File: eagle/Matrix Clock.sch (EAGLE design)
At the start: 48 parts, among them IC1 MEGA32-A, IC2 LM1117IMPX-3.3, IC3 DS1307Z, IC4 MAX7219CWG, IC5 MAX7219CWG, IC6 MAX7219CWG, IC7 MAX7219CWG, Q1 32768, Q2 16MHz, X1 MINI-USB-SCHIELD-32005-301

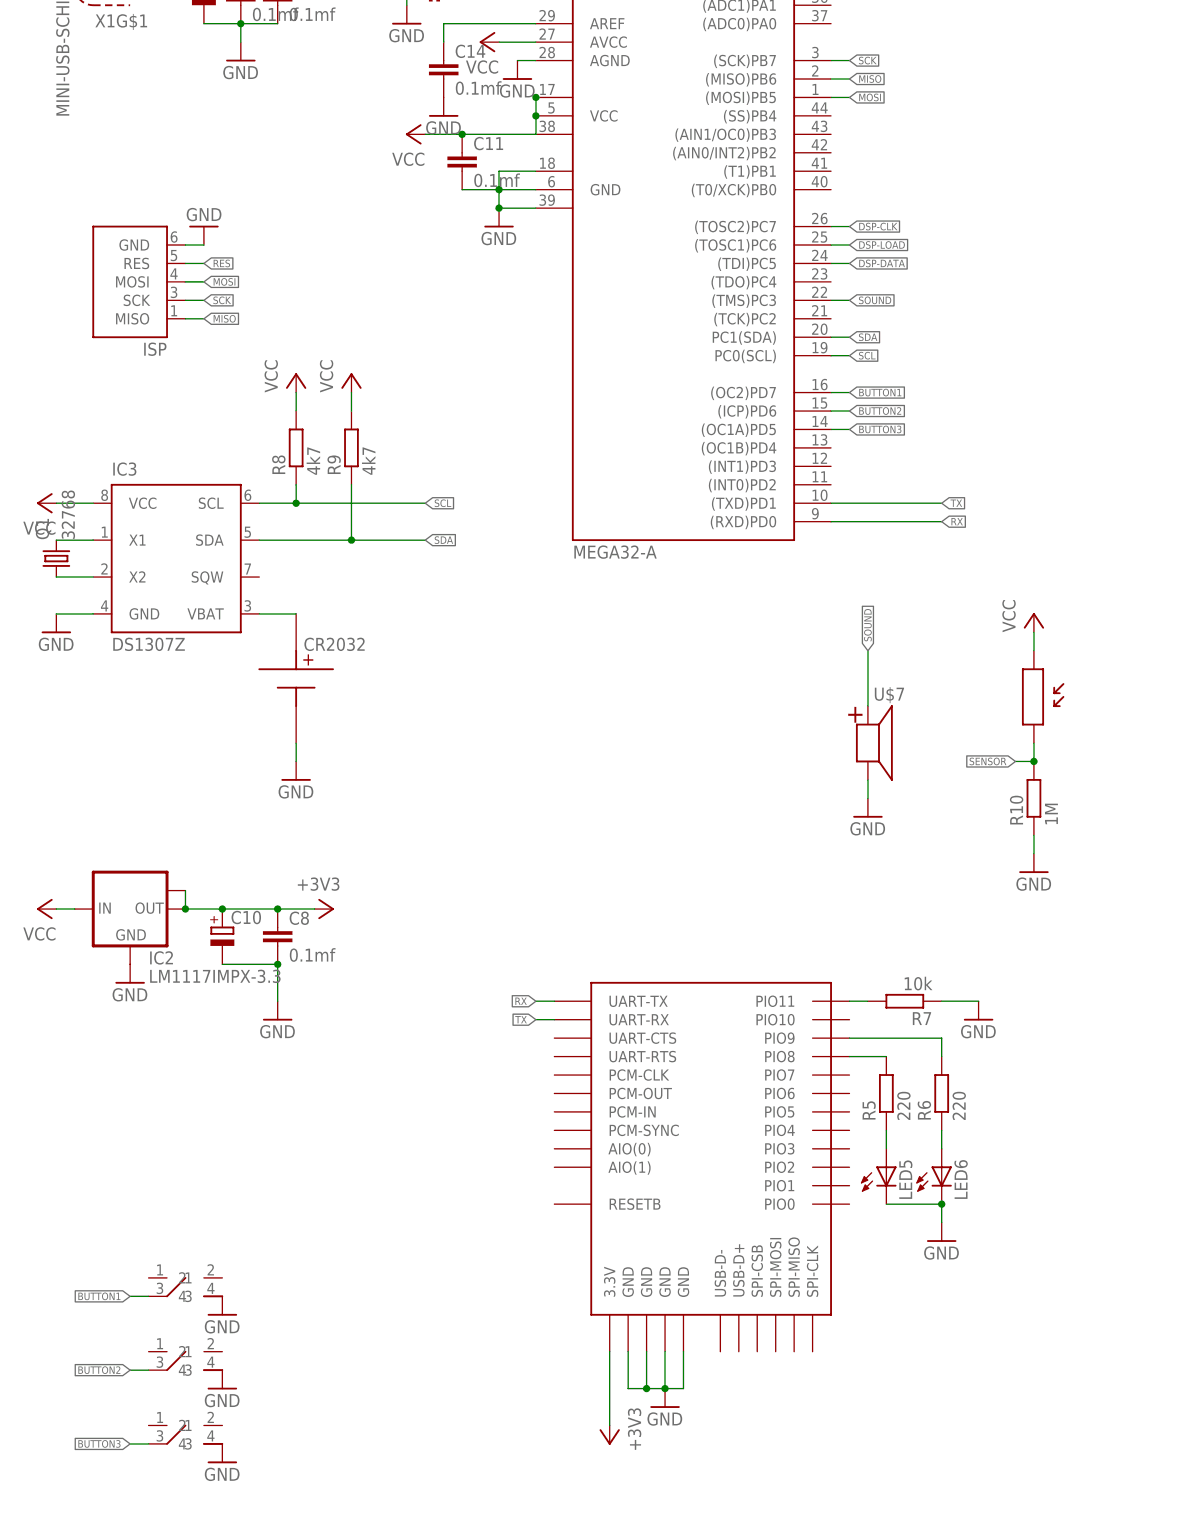
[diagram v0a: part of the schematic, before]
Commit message: Started clock firmware
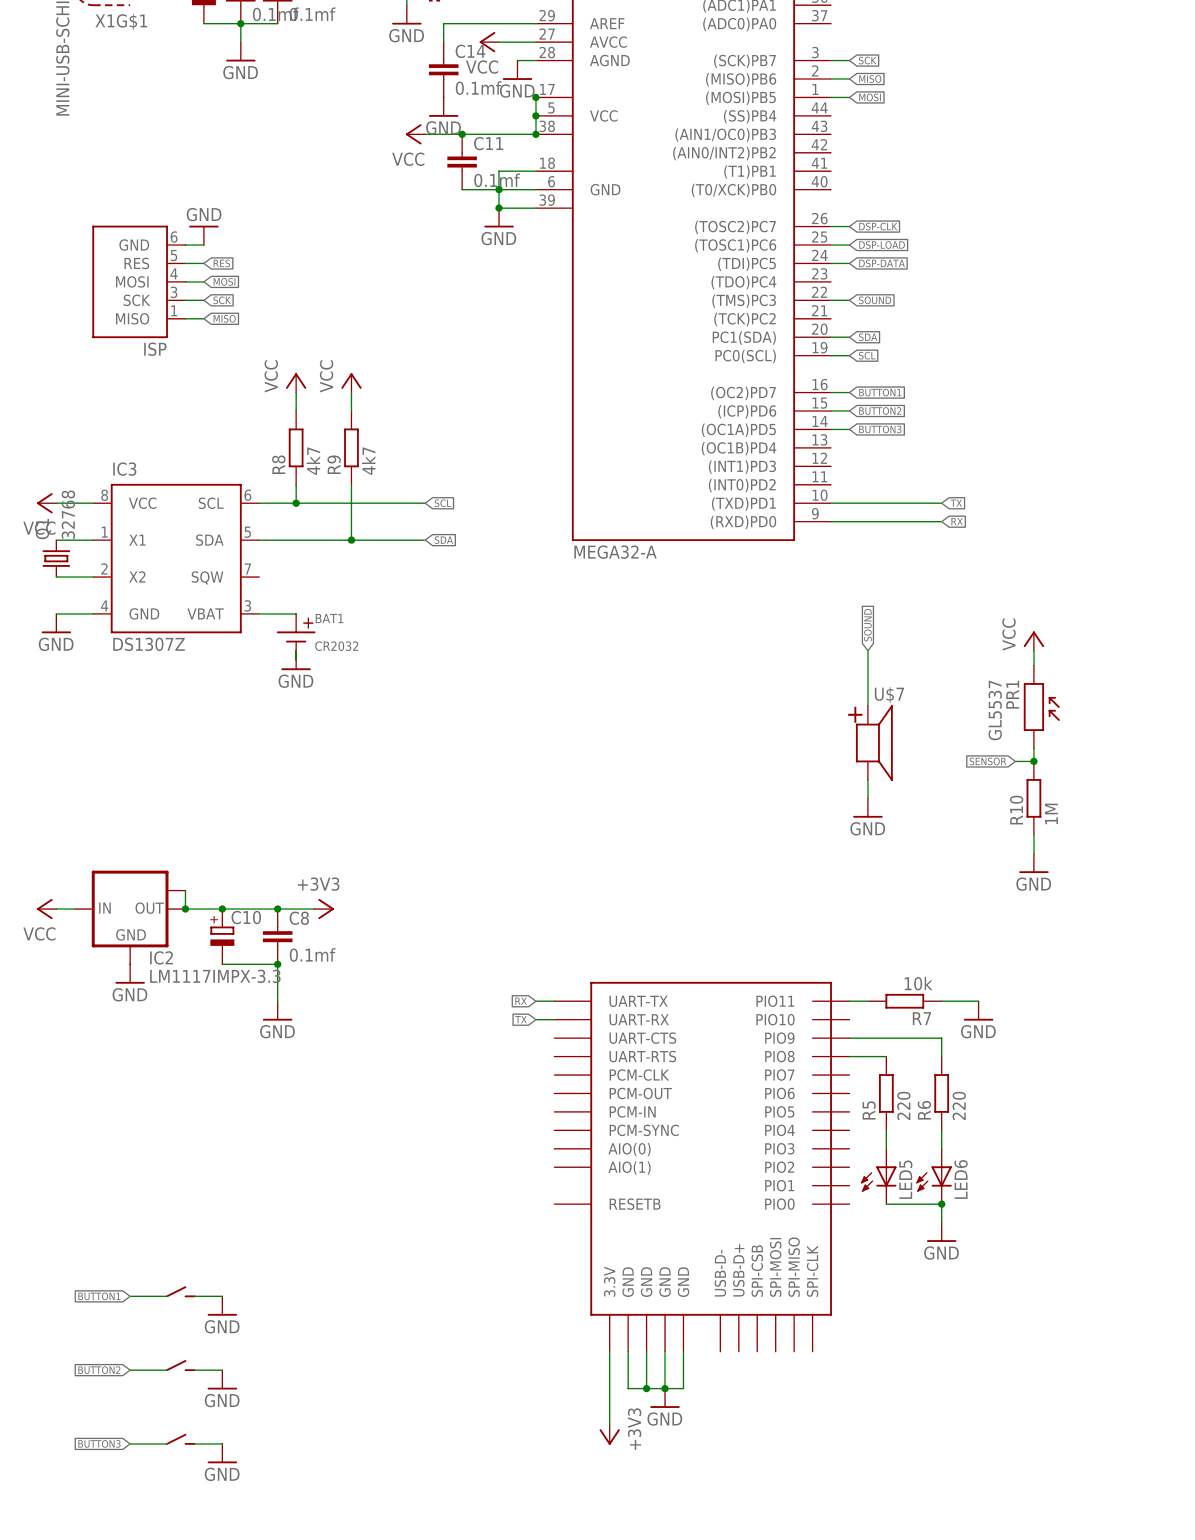
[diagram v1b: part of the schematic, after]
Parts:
- removed U$12: GL5537, misc:GL5537
- removed U$5: CR2032, misc:CR2032
- added BAT1: CR2032, misc:CR2032
- added PR1: GL5537, misc:GL5537
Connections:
- net GND: now also BAT1.GND; no longer U$5.GND
- net N$3: now also BAT1.VBAT; no longer U$5.VBAT
- net SENSOR: now also PR1.P$2; no longer U$12.P$2
- net VCC: now also PR1.P$1; no longer U$12.P$1
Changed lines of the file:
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@@
 <part name="IC2" library="lm1117" deviceset="LM1117IMPX-*" device="" technology="3.3"/>
 <part name="U$1" library="bc417" deviceset="BTM400_6B" device=""/>
-<part name="U$5" library="misc" deviceset="CR2032" device=""/>
+<part name="BAT1" library="misc" deviceset="CR2032" device=""/>
 <part name="U$7" library="misc" deviceset="HC0905" device=""/>
 <part name="U$9" library="misc" deviceset="IT1188E" device=""/>
@@
 <part name="GND20" library="supply1" deviceset="GND" device=""/>
 <part name="GND21" library="supply1" deviceset="GND" device=""/>
-<part name="U$12" library="misc" deviceset="GL5537" device=""/>
+<part name="PR1" library="misc" deviceset="GL5537" device=""/>
 <part name="R10" library="rcl" deviceset="R-EU_" device="R0805" value="1M"/>
 <part name="GND22" library="supply1" deviceset="GND" device=""/>
@@
 <instance part="IC2" gate="G$1" x="12.7" y="-147.32"/>
 <instance part="U$1" gate="G$1" x="91.44" y="-185.42"/>
-<instance part="U$5" gate="G$1" x="35.56" y="-114.3"/>
+<instance part="BAT1" gate="G$1" x="35.56" y="-109.22"/>
 <instance part="U$7" gate="G$1" x="114.3" y="-127"/>
 <instance part="U$9" gate="G$1" x="20.32" y="-198.12"/>
@@
 <instance part="GND8" gate="1" x="22.86" y="-53.34" rot="R180"/>
 <instance part="GND9" gate="1" x="114.3" y="-134.62"/>
-<instance part="GND10" gate="1" x="35.56" y="-129.54"/>
+<instance part="GND10" gate="1" x="35.56" y="-114.3"/>
 <instance part="GND11" gate="1" x="12.7" y="-157.48"/>
 <instance part="P+7" gate="VCC" x="0" y="-147.32" rot="R90"/>
@@
 <instance part="GND20" gate="1" x="33.02" y="-162.56"/>
 <instance part="GND21" gate="1" x="27.94" y="-30.48"/>
-<instance part="U$12" gate="G$1" x="137.16" y="-121.92"/>
+<instance part="PR1" gate="G$1" x="137.16" y="-119.38" rot="R270"/>
 <instance part="R10" gate="G$1" x="137.16" y="-132.08" rot="R90"/>
 <instance part="GND22" gate="1" x="137.16" y="-142.24"/>
-<instance part="P+12" gate="VCC" x="137.16" y="-106.68"/>
+<instance part="P+12" gate="VCC" x="137.16" y="-109.22"/>
 <instance part="C11" gate="G$1" x="58.42" y="-43.18"/>
 <instance part="C12" gate="G$1" x="33.02" y="-20.32"/>
@@
 </segment>
 <segment>
-<pinref part="U$5" gate="G$1" pin="GND"/>
+<pinref part="BAT1" gate="G$1" pin="GND"/>
 <pinref part="GND10" gate="1" pin="GND"/>
-<wire x1="35.56" y1="-124.46" x2="35.56" y2="-127" width="0.1524" layer="91"/>
+<wire x1="35.56" y1="-113.03" x2="35.56" y2="-111.76" width="0.1524" layer="91"/>
 </segment>
 <segment>
@@
 <pinref part="U$11" gate="G$1" pin="4"/>
 <pinref part="GND16" gate="1" pin="GND"/>
+<wire x1="25.4" y1="-220.98" x2="21.59" y2="-220.98" width="0.1524" layer="91"/>
 </segment>
 <segment>
 <pinref part="U$9" gate="G$1" pin="4"/>
 <pinref part="GND18" gate="1" pin="GND"/>
+<wire x1="25.4" y1="-200.66" x2="21.59" y2="-200.66" width="0.1524" layer="91"/>
 </segment>
 <segment>
 <pinref part="U$10" gate="G$1" pin="4"/>
 <pinref part="GND17" gate="1" pin="GND"/>
+<wire x1="25.4" y1="-210.82" x2="21.59" y2="-210.82" width="0.1524" layer="91"/>
 </segment>
 <segment>
@@
 <pinref part="C11" gate="G$1" pin="1"/>
 <junction x="58.42" y="-40.64"/>
+<junction x="68.58" y="-40.64"/>
 </segment>
 <segment>
@@
 </segment>
 <segment>
-<pinref part="U$12" gate="G$1" pin="P$1"/>
+<pinref part="PR1" gate="G$1" pin="P$1"/>
 <pinref part="P+12" gate="VCC" pin="VCC"/>
-<wire x1="137.16" y1="-109.22" x2="137.16" y2="-111.76" width="0.1524" layer="91"/>
+<wire x1="137.16" y1="-111.76" x2="137.16" y2="-113.792" width="0.1524" layer="91"/>
 </segment>
 <segment>
@@
 <segment>
 <pinref part="U$9" gate="G$1" pin="3"/>
-<wire x1="15.24" y1="-200.66" x2="12.7" y2="-200.66" width="0.1524" layer="91"/>
+<wire x1="17.78" y1="-200.66" x2="12.7" y2="-200.66" width="0.1524" layer="91"/>
 <label x="12.7" y="-200.66" size="1.016" layer="95" rot="MR0" xref="yes"/>
 </segment>
@@
 <segment>
 <pinref part="U$10" gate="G$1" pin="3"/>
-<wire x1="15.24" y1="-210.82" x2="12.7" y2="-210.82" width="0.1524" layer="91"/>
+<wire x1="17.78" y1="-210.82" x2="12.7" y2="-210.82" width="0.1524" layer="91"/>
 <label x="12.7" y="-210.82" size="1.016" layer="95" rot="MR0" xref="yes"/>
 </segment>
@@
 <segment>
 <pinref part="U$11" gate="G$1" pin="3"/>
-<wire x1="15.24" y1="-220.98" x2="12.7" y2="-220.98" width="0.1524" layer="91"/>
+<wire x1="17.78" y1="-220.98" x2="12.7" y2="-220.98" width="0.1524" layer="91"/>
 <label x="12.7" y="-220.98" size="1.016" layer="95" rot="MR0" xref="yes"/>
 </segment>
@@
 <segment>
 <pinref part="IC3" gate="G$1" pin="VBAT"/>
-<pinref part="U$5" gate="G$1" pin="VBAT"/>
+<pinref part="BAT1" gate="G$1" pin="VBAT"/>
 <wire x1="30.48" y1="-106.68" x2="35.56" y2="-106.68" width="0.1524" layer="91"/>
 </segment>
@@
 <net name="SENSOR" class="0">
 <segment>
-<pinref part="U$12" gate="G$1" pin="P$2"/>
+<pinref part="PR1" gate="G$1" pin="P$2"/>
 <pinref part="R10" gate="G$1" pin="2"/>
-<wire x1="137.16" y1="-127" x2="137.16" y2="-124.46" width="0.1524" layer="91"/>
+<wire x1="137.16" y1="-127" x2="137.16" y2="-125.222" width="0.1524" layer="91"/>
 <wire x1="137.16" y1="-127" x2="134.62" y2="-127" width="0.1524" layer="91"/>
 <junction x="137.16" y="-127"/>
